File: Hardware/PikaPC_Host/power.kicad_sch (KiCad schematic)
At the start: 32 parts, among them U1 PPC403GA, U2 ATF1508AS

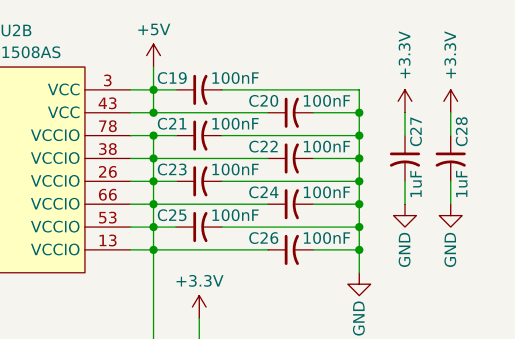
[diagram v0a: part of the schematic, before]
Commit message: Host card PCB layout
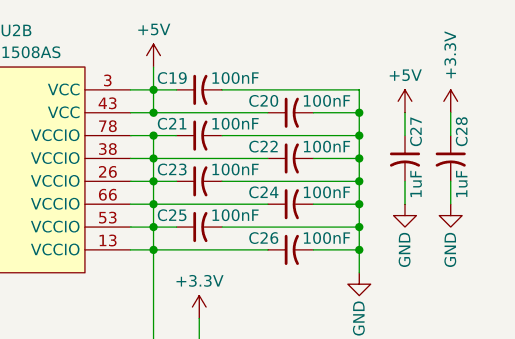
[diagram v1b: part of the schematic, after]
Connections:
- net +3.3V: no longer C27.1
- net +5V: now also C27.1
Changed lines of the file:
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@@
 	)
 	(symbol
+		(lib_id "power:+5V")
+		(at 195.58 30.48 0)
+		(unit 1)
+		(exclude_from_sim no)
+		(in_bom yes)
+		(on_board yes)
+		(dnp no)
+		(fields_autoplaced yes)
+		(property "Reference" "#PWR017"
+			(at 195.58 34.29 0)
+			(effects
+				(font
+					(size 1.27 1.27)
+				)
+				(hide yes)
+			)
+		)
+		(property "Value" "+5V"
+			(at 195.58 26.3469 0)
+			(effects
+				(font
+					(size 1.27 1.27)
+				)
+			)
+		)
+		(property "Footprint" ""
+			(at 195.58 30.48 0)
+			(effects
+				(font
+					(size 1.27 1.27)
+				)
+				(hide yes)
+			)
+		)
+		(property "Datasheet" ""
+			(at 195.58 30.48 0)
+			(effects
+				(font
+					(size 1.27 1.27)
+				)
+				(hide yes)
+			)
+		)
+		(property "Description" "Power symbol creates a global label with name \"+5V\""
+			(at 195.58 30.48 0)
+			(effects
+				(font
+					(size 1.27 1.27)
+				)
+				(hide yes)
+			)
+		)
+		(pin "1"
+		)
+		(instances
+			(project "PikaPC_Host"
+				(path "/6a60ec03-e28d-46ba-8906-3c4e1028fc94/fa2fd65c-4f78-487f-96bd-13f5cb66f892"
+					(reference "#PWR017")
+					(unit 1)
+				)
+			)
+		)
+	)
+	(symbol
 		(lib_id "Device:C_Small_US")
 		(at 195.58 35.56 0)
@@
 					(unit 1)
 				)
-			)
-		)
-	)
-	(symbol
-		(lib_id "power:+3.3V")
-		(at 195.58 30.48 0)
-		(unit 1)
-		(exclude_from_sim no)
-		(in_bom yes)
-		(on_board yes)
-		(dnp no)
-		(property "Reference" "#PWR017"
-			(at 195.58 34.29 0)
-			(effects
-				(font
-					(size 1.27 1.27)
-				)
-				(hide yes)
-			)
-		)
-		(property "Value" "+3.3V"
-			(at 195.58 24.13 90)
-			(effects
-				(font
-					(size 1.27 1.27)
-				)
-			)
-		)
-		(property "Footprint" ""
-			(at 195.58 30.48 0)
-			(effects
-				(font
-					(size 1.27 1.27)
-				)
-				(hide yes)
-			)
-		)
-		(property "Datasheet" ""
-			(at 195.58 30.48 0)
-			(effects
-				(font
-					(size 1.27 1.27)
-				)
-				(hide yes)
-			)
-		)
-		(property "Description" "Power symbol creates a global label with name \"+3.3V\""
-			(at 195.58 30.48 0)
-			(effects
-				(font
-					(size 1.27 1.27)
-				)
-				(hide yes)
-			)
-		)
-		(pin "1"
-		)
-		(instances
-			(project "PikaPC_Host"
-				(path "/6a60ec03-e28d-46ba-8906-3c4e1028fc94/fa2fd65c-4f78-487f-96bd-13f5cb66f892"
-					(reference "#PWR017")
-					(unit 1)
-				)

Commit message: Host card PCB layout
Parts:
- added C50, C51, C52, C53: 10uF, Capacitor_SMD:CP_Elec_4x5.7, symbol Device:C_Polarized_Small_US
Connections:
- net +3.3V: now also C52.1, C53.1
- net +5V: now also C50.1, C51.1
- net GND: now also C50.2, C51.2, C52.2, C53.2

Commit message: Annotate & prep for output - Host & KBC
add gerber output to gitignore
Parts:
- C1, C10, C11, C12, C13, C14, C19, C2, C20, C21, C22, C23, C24, C25, C26, C3, C4, C5, C6, C7, C8, C9: Mouser (none) -> 187-CL21B104KACNNNC
- C15, C16, C17, C18, C27, C28: Mouser (none) -> 187-CL21B105KOFNNNG
